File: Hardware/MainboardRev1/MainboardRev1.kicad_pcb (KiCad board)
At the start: 2 copper layers, 92 x 92 mm, 202 parts, among them J1 MAIN_BATT: 1586038-2, J10 Switch_3, J11 Switch_2, J12 Switch_4, J2 BACKUP_BATT: 1586038-2, J3 Servo_Control, J4 EMATCH_1: 1586038-2, J5 EMATCH_2: 1586038-2, J6 Stratologger_PWR: 1586038-2, J7 Stratologger_DATA, J8 0733910320 [915MHz SMA], J9 Switch_1, Q1 SSM3J328R, Q10 SSM3J328R, Q11 NTR4003, Q12 NTR4003, Q13 NTR4003, Q14 SSM3J328R, Q15 NTR4003, Q16 SSM3J328R, Q17 SSM3J328R, Q18 NTR4003, Q19 NTR4003, Q2 SSM3J328R, Q20 SIS612EDNT-T1-GE3, Q21 SIS612EDNT-T1-GE3, Q22 NTR4003, Q23 NTR4003, Q24 NTR4003, Q25 SSM3J328R, Q26 NTR4003, Q3 SSM3J328R, Q4 SSM3J328R, Q5 NTR4003, Q6 NTR4003, Q7 NTR4003, Q8 SSM3J328R, Q9 NTR4003, SW1 EG2201A [DPDT], U1 LT6703-3, U10 LTC4358, U11 Teensy3.6, U12 ABPMANN030PG2A3, U13 LSM9DS1, U14 LIS331HH, U15 BME280, U16 CCS811, U17 ublox_max-m8q, U18 RFM69HCW, U2 LTC3605, U3 LTC4358, U4 LTC4358, U5 LDL1117S50R, U6 LDL1117S33R, U7 LTC2992, U8 LDL1117S33R, U9 LTC2992

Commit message: Components placed. Needs to be routed.
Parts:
- removed C1: 47uF, Capacitors_SMD:C_1210_HandSoldering
- added C36: 10nF, Capacitors_SMD:C_0603_HandSoldering, B.Cu at (72.4, 80.0)
- added J13: EXTRA_5V, Dans_Parts:CONN_2POS_VERT_TE_CONN_LOCK_5-103669-1, F.Cu at (114.7, 110.7)
- added J14: EXTRA_3V3, Dans_Parts:CONN_2POS_VERT_TE_CONN_LOCK_5-103669-1, F.Cu at (114.7, 119.5)
- added MH1: Mounting Hole, Dans_Parts:Mounting_Hole_3.50mm, F.Cu at (54.0, 62.0)
- added MH2: Mounting Hole, Dans_Parts:Mounting_Hole_3.50mm, F.Cu at (138.0, 62.0)
- added MH3: Mounting Hole, Dans_Parts:Mounting_Hole_3.50mm, F.Cu at (54.0, 130.0)
- added MH4: Mounting Hole, Dans_Parts:Mounting_Hole_3.50mm, F.Cu at (138.0, 130.0)
- C10, C11, C12, C13, C2, C3, C33, C34, C35, C4, C5, C6, C7, C8, C9, D1, D11, D2, D3, D4, D5, L1, Q1, Q10, Q11, Q12, Q13, Q14, Q15, Q2, Q3, Q4, Q5, Q6, Q7, Q8, R1, R10, R11, R12, R13, R14, R15, R16, R17, R18, R19, R2, R21, R22, R23, R25, R28, R3, R34, R4, R44, R45, R5, R6, R7, R78, R8, R84, R85, R86, R87, R88, R89, R9, R90, R91, U1, U2, U3, U4: moved to B.Cu
- C14, C19: value 1uF -> 47uF; footprint Capacitors_SMD:C_0603_HandSoldering -> Capacitors_SMD:C_1210_HandSoldering; moved to B.Cu
- C15, C20: value 4.7uF -> 0.1uF
- C16, C17, C18, C21: value 4.7uF -> 47uF; footprint Capacitors_SMD:C_0603_HandSoldering -> Capacitors_SMD:C_1210_HandSoldering; moved to B.Cu
- C23: value 10000pF -> 47uF; footprint Capacitors_SMD:C_0603_HandSoldering -> Capacitors_SMD:C_1210_HandSoldering; moved to B.Cu
- C24: value 0.1uF -> 10000pF
- C25: value 100nF -> 0.1uF
- C26: value 0.1uF -> 100nF
- C32: value 10nF -> 0.1uF
- J1: value MAIN_BATT: 1586038-2 -> BACKUP_BATT: 1586038-2
- J10, J11, J12, J9: footprint Dans_Parts:Molex_Microfit3_Header_02x01_Straight -> Dans_Parts:CONN_2POS_VERT_TE_CONN_LOCK_5-103669-1
- J2: value BACKUP_BATT: 1586038-2 -> MAIN_BATT: 1586038-2
- R56: value 10k -> 45.2k; moved to B.Cu
- R57: value 45.2k -> 11.3k; moved to B.Cu
- R58: value 11.3k -> R
- R59: value 10k -> R
- R60: value 45.2k -> R
- R61, R66: value 11.3k -> 45.2k; moved to B.Cu
- R62: value R -> 11.3k; moved to B.Cu
- R63, R64: value R -> 10k
- R65: value 45.2k -> 10k
- R67: value 10k -> 11.3k; moved to B.Cu
- U10: footprint Housings_SSOP:TSSOP-14-1EP_4.4x5mm_Pitch0.65mm -> Housings_SSOP:HTSSOP-16-1EP_4.4x5mm_Pitch0.65mm; moved to B.Cu
- U5, U6, U8: footprint TO_SOT_Packages_SMD:SOT-223 -> Dans_Parts:SOT-223_Tab_Pin_2; moved to B.Cu
- moved R76 270.0 mm to (52.8, 97.7), turned to 180 degrees
- moved R75 262.0 mm to (56.4, 100.8), turned to 270 degrees
- moved J7 259.1 mm to (60.4, 129.9), turned to 270 degrees
- moved C35 257.8 mm to (72.4, 87.7)
- moved R78 254.1 mm to (58.0, 126.6), turned to 90 degrees
- moved R77 253.8 mm to (56.4, 95.2), turned to 90 degrees
- moved Q25 251.5 mm to (53.3, 100.8), turned to 180 degrees
- moved Q26 251.2 mm to (53.3, 94.9), turned to 180 degrees
- moved R59 250.4 mm to (53.1, 72.4), turned to 180 degrees
- moved R89 249.9 mm to (72.4, 81.5)
- moved R84 249.5 mm to (79.8, 92.5), turned to 180 degrees
- moved R60 246.5 mm to (53.1, 78.0), turned to 180 degrees
- moved R86 245.6 mm to (79.8, 89.4), turned to 180 degrees
- moved C34 244.0 mm to (79.8, 83.6)
- moved R85 242.9 mm to (79.8, 85.1), turned to 180 degrees
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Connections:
- C14 pad 1: Net-(C14-Pad1) -> BATTERY_PWR_MSMT
- C15 pad 1: LDO_FEED -> Net-(C15-Pad1)
- C17 pad 1: +5V_MSMT -> LDO_FEED
- C18 pad 1: +3.3V_MSMT -> +5V_MSMT
- C19 pad 1: Net-(C19-Pad1) -> +3.3V_MSMT
- C2 pad 1: MAIN_BATT -> BACKUP_BATT
- C20 pad 1: STARTUP_BATT -> Net-(C20-Pad1)
- C21 pad 1: +3.3V_STARTUP -> STARTUP_BATT
- C22 pad 1: Net-(C22-Pad1) -> +3.3V_STARTUP
- C23 pad 1: LSM_CAP -> Net-(C23-Pad1)
- C24 pad 1: Net-(C24-Pad1) -> LSM_CAP
- C25 pad 1: LSM_C1 -> Net-(C25-Pad1)
- C26 pad 1: Net-(C26-Pad1) -> LSM_C1
- C3 pad 1: BACKUP_BATT -> MAIN_BATT
- D1 pad 1: MAIN_BATT -> BACKUP_BATT
- D10 pad 2: +5V -> Net-(D10-Pad2)
- D11 pad 1: Net-(C22-Pad1) -> Net-(C23-Pad1)
- D2 pad 1: BACKUP_BATT -> MAIN_BATT
- D6 pad 2: +5V -> Net-(D6-Pad2)
- J10 pad 1: Net-(C33-Pad1) -> Net-(C34-Pad1)
- J11 pad 1: Net-(C34-Pad1) -> Net-(C35-Pad1)
- J12 pad 1: Net-(C35-Pad1) -> Net-(C36-Pad1)
- J3 pad 2: Net-(C22-Pad1) -> Net-(C23-Pad1)
- J9 pad 1: Net-(C32-Pad1) -> Net-(C33-Pad1)
- Q1 pad 2: MAIN_BATT -> BACKUP_BATT
- Q12 pad 3: Net-(Q12-Pad3) -> Net-(D6-Pad1)
- Q13 pad 3: Net-(Q13-Pad3) -> Net-(D10-Pad1)
- Q2 pad 2: BACKUP_BATT -> MAIN_BATT
- Q3 pad 2: MAIN_BATT -> BACKUP_BATT
- Q4 pad 2: BACKUP_BATT -> MAIN_BATT
- Q5 pad 1: MAIN_BATT_EN -> BACKUP_BATT_EN
- Q6 pad 1: BACKUP_BATT_EN -> MAIN_BATT_EN
- R12 pad 1: MAIN_BATT_EN -> +3.3V_STARTUP
- R12 pad 2: GND -> BACKUP_BATT_EN
- R13 pad 1: +3.3V_STARTUP -> MAIN_BATT_EN
- R13 pad 2: BACKUP_BATT_EN -> GND
- R24 pad 1: Net-(C14-Pad1) -> Net-(C15-Pad1)
- R31 pad 1: Net-(C19-Pad1) -> Net-(C20-Pad1)
- R35 pad 1: +5V -> +3.3V
- R35 pad 2: +5V_MSMT -> +3.3V_MSMT
- R36 pad 1: +3.3V -> +5V
- R36 pad 2: +3.3V_MSMT -> +5V_MSMT
- R39 pad 1: Net-(D6-Pad1) -> +5V
- R39 pad 2: Net-(Q12-Pad3) -> Net-(D6-Pad2)
- R43 pad 1: Net-(D10-Pad1) -> +5V
- R43 pad 2: Net-(Q13-Pad3) -> Net-(D10-Pad2)
- R56 pad 1: +3.3V -> MAIN_BATT
- R56 pad 2: SENSORS_SCL -> MAIN_BATT_ANLG
- R57 pad 1: MAIN_BATT -> MAIN_BATT_ANLG
- R57 pad 2: MAIN_BATT_ANLG -> MAIN_BATT_READ_EN
- R58 pad 1: MAIN_BATT_ANLG -> Net-(D14-Pad2)
- R58 pad 2: MAIN_BATT_READ_EN -> +5V
- R59 pad 1: +3.3V -> Net-(D15-Pad2)
- R59 pad 2: SENSORS_SDA -> +5V
- R6 pad 1: MAIN_BATT -> BACKUP_BATT
- R60 pad 1: EMATCH_1_CHECK -> Net-(D16-Pad2)
- R60 pad 2: EMATCH_1_ANLG -> +5V
- R61 pad 1: EMATCH_1_ANLG -> EMATCH_1_CHECK
- R61 pad 2: GND -> EMATCH_1_ANLG
- R62 pad 1: Net-(D14-Pad2) -> EMATCH_1_ANLG
- R62 pad 2: +5V -> GND
- R63 pad 1: Net-(D15-Pad2) -> GND
- R63 pad 2: +5V -> LED_GREEN
- R64 pad 1: Net-(D16-Pad2) -> GND
- R64 pad 2: +5V -> LED_BLUE
- R65 pad 1: EMATCH_2_CHECK -> +3.3V
- R65 pad 2: EMATCH_2_ANLG -> LED_RED
- R66 pad 1: EMATCH_2_ANLG -> EMATCH_2_CHECK
- R66 pad 2: GND -> EMATCH_2_ANLG
- R67 pad 1: GND -> EMATCH_2_ANLG
- R67 pad 2: LED_GREEN -> GND
- R68 pad 1: GND -> +3.3V
- R68 pad 2: LED_BLUE -> SENSORS_SCL
- R69 pad 2: LED_RED -> SENSORS_SDA
- R70 pad 1: Net-(C24-Pad1) -> Net-(C25-Pad1)
- R71 pad 1: Net-(C26-Pad1) -> Net-(C27-Pad1)
- R72 pad 1: Net-(C27-Pad1) -> Net-(C28-Pad1)
- R73 pad 1: Net-(C28-Pad1) -> Net-(C29-Pad1)
- R74 pad 1: Net-(C29-Pad1) -> Net-(C30-Pad1)
- R79 pad 1: Net-(C30-Pad1) -> Net-(C31-Pad1)
- R8 pad 1: BACKUP_BATT -> MAIN_BATT
- R81 pad 1: Net-(C31-Pad1) -> Net-(C32-Pad1)
- R84 pad 2: Net-(C32-Pad1) -> Net-(C33-Pad1)
- R85 pad 2: Net-(C33-Pad1) -> Net-(C34-Pad1)
- R86 pad 2: Net-(C32-Pad1) -> Net-(C33-Pad1)
- R87 pad 2: Net-(C33-Pad1) -> Net-(C34-Pad1)
- R88 pad 2: Net-(C34-Pad1) -> Net-(C35-Pad1)
- R89 pad 2: Net-(C35-Pad1) -> Net-(C36-Pad1)
- R90 pad 2: Net-(C34-Pad1) -> Net-(C35-Pad1)
- R91 pad 2: Net-(C35-Pad1) -> Net-(C36-Pad1)
- U10 pad 10: Net-(U10-Pad10) -> Net-(C23-Pad1)
- U10 pad 11: Net-(Q14-Pad3) -> Net-(U10-Pad11)
- U10 pad 15: Net-(C22-Pad1) -> Net-(Q14-Pad3)
- U10 pad 7: GND -> Net-(U10-Pad7)
- U10 pad 8: Net-(C22-Pad1) -> GND
- U10 pad 9: Net-(C22-Pad1) -> Net-(C23-Pad1)
- U12 pad 2: Net-(C26-Pad1) -> Net-(C27-Pad1)
- U13 pad 1: Net-(C24-Pad1) -> Net-(C25-Pad1)
- U13 pad 22: Net-(C24-Pad1) -> Net-(C25-Pad1)
- U13 pad 23: Net-(C24-Pad1) -> Net-(C25-Pad1)
- U13 pad 3: Net-(C24-Pad1) -> Net-(C25-Pad1)
- U14 pad 1: Net-(C27-Pad1) -> Net-(C28-Pad1)
- U14 pad 14: Net-(C27-Pad1) -> Net-(C28-Pad1)
- U14 pad 15: Net-(C27-Pad1) -> Net-(C28-Pad1)
- U15 pad 2: Net-(C28-Pad1) -> Net-(C29-Pad1)
- U15 pad 6: Net-(C28-Pad1) -> Net-(C29-Pad1)
- U15 pad 8: Net-(C28-Pad1) -> Net-(C29-Pad1)
- U16 pad 6: Net-(C29-Pad1) -> Net-(C30-Pad1)
- U17 pad 6: Net-(C30-Pad1) -> Net-(C31-Pad1)
- U17 pad 7: Net-(C30-Pad1) -> Net-(C31-Pad1)
- U17 pad 8: Net-(C30-Pad1) -> Net-(C31-Pad1)
- U17 pad 9: Net-(C30-Pad1) -> Net-(C31-Pad1)
- U18 pad 13: Net-(C31-Pad1) -> Net-(C32-Pad1)
- U3 pad 10: Net-(U3-Pad10) -> BATTERY_PWR_MSMT
- U3 pad 11: Net-(Q3-Pad3) -> Net-(U3-Pad11)
- U3 pad 15: BATTERY_PWR_MSMT -> Net-(Q3-Pad3)
- U3 pad 16: (no net) -> Net-(Q3-Pad3)
- U3 pad 17: (no net) -> BATTERY_PWR_MSMT
- U3 pad 7: GND -> Net-(U3-Pad7)
- U3 pad 8: BATTERY_PWR_MSMT -> GND
- U4 pad 10: Net-(U4-Pad10) -> BATTERY_PWR_MSMT
- U4 pad 11: Net-(Q4-Pad3) -> Net-(U4-Pad11)
- U4 pad 15: BATTERY_PWR_MSMT -> Net-(Q4-Pad3)
- U4 pad 16: (no net) -> Net-(Q4-Pad3)
- U4 pad 17: (no net) -> BATTERY_PWR_MSMT
- U4 pad 7: GND -> Net-(U4-Pad7)
- U4 pad 8: BATTERY_PWR_MSMT -> GND
- U7 pad 7: Net-(C14-Pad1) -> Net-(C15-Pad1)
- U7 pad 8: Net-(C14-Pad1) -> Net-(C15-Pad1)
- U9 pad 1: +5V -> +3.3V
- U9 pad 15: +3.3V_MSMT -> +5V_MSMT
- U9 pad 16: +3.3V -> +5V
- U9 pad 2: +5V_MSMT -> +3.3V_MSMT
- U9 pad 7: Net-(C19-Pad1) -> Net-(C20-Pad1)
- U9 pad 8: Net-(C19-Pad1) -> Net-(C20-Pad1)
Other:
- outline, holes or cut-outs redrawn
- copper layers 2 -> 4
- net class 5A_External added: clearance 0.2, trace_width 1.4, via_dia 0.6, via_drill 0.4
- board text added: "3.3V"
- board text added: "5V"
- board text added: "6.5V"
- board text added: "915 MHz ANT"
- board text added: "Backup Batt"
- board text added: "Batt"
- board text added: "Ematch 1 ARMED"
- board text added: "Ematch 2 ARMED"
- board text added: "Extra 3V3"
- board text added: "Extra 5V"
- board text added: "GPS Lock"
- board text added: "Main Batt"
- board text added: "OFF"
- board text added: "ON"
- board text added: "SW1"
- board text added: "SW2"
- board text added: "SW3"
- board text added: "SW4"
- board text added: "Servo Motor"
- board text added: "Strato Data"
- board text added: "Strato Power"

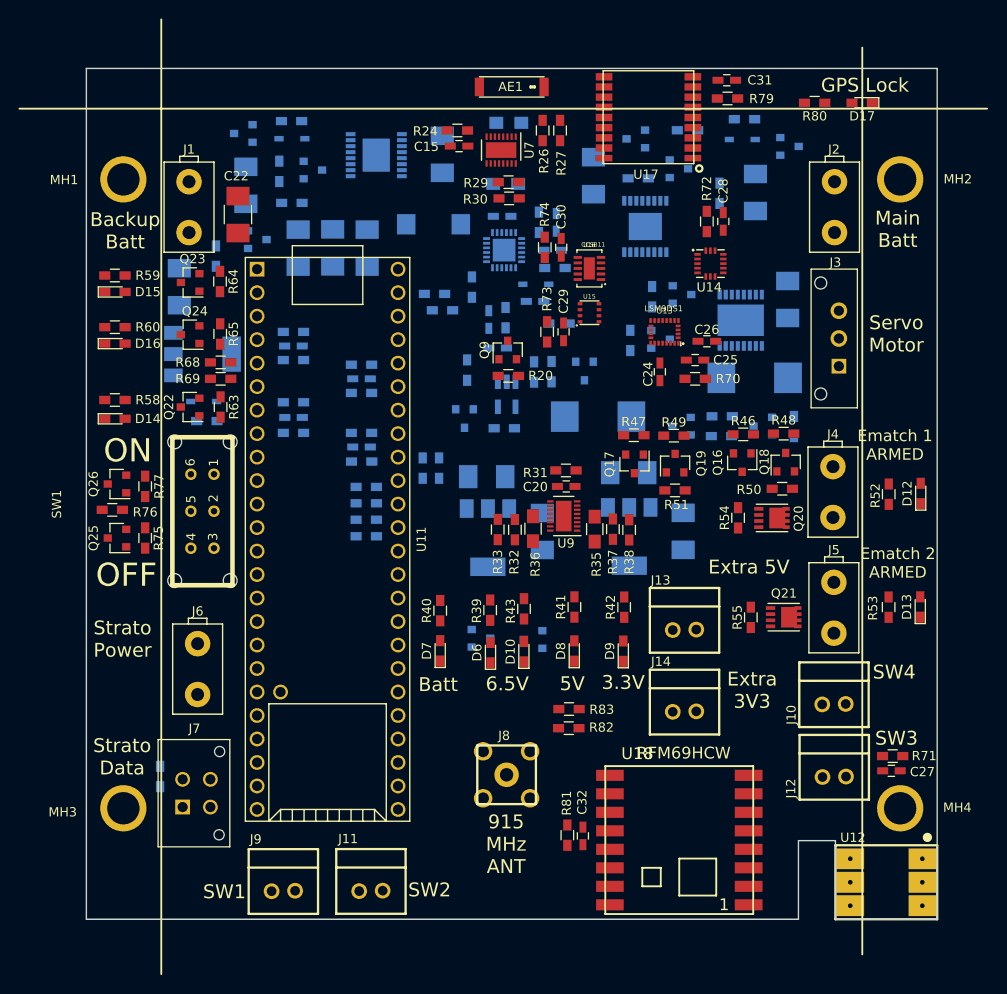
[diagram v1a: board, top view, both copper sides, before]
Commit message: Added to silkscreen. Updated schematic pdf
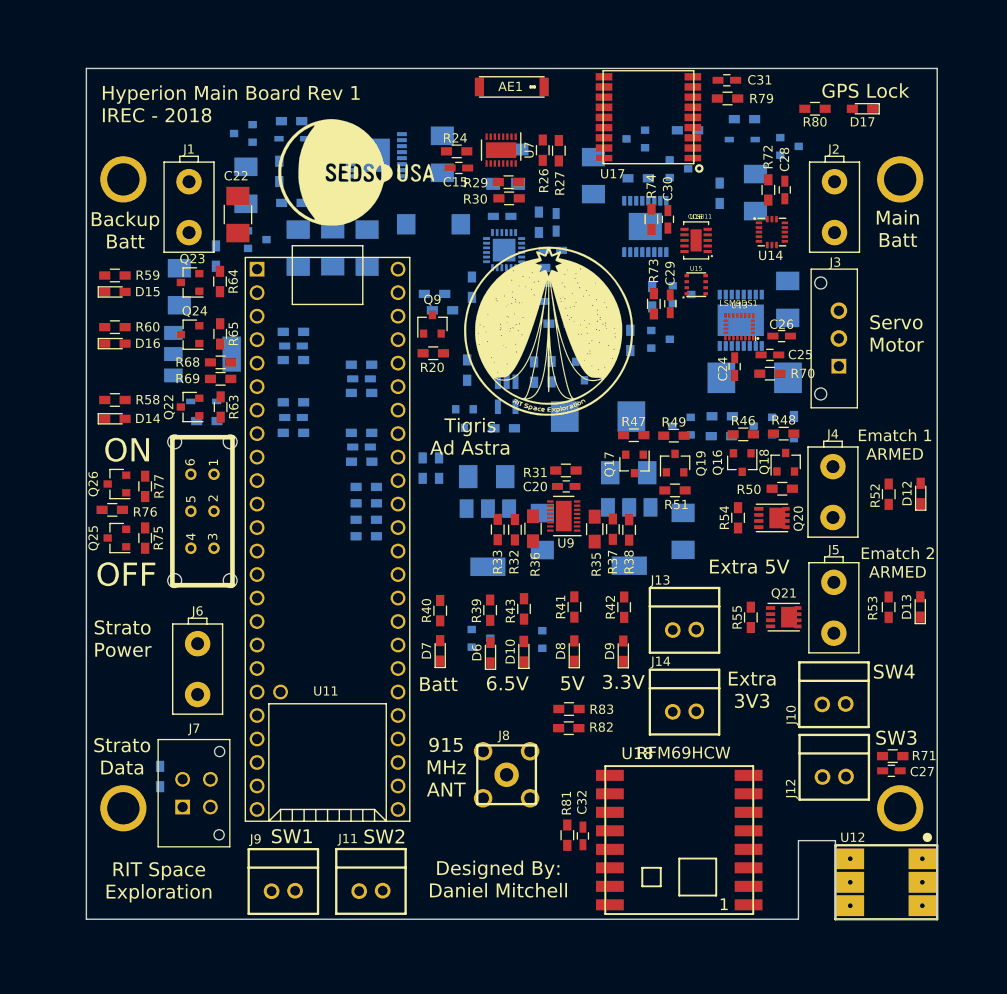
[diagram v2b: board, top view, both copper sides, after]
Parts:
- added G***: LOGO, Media:SPEX_KiCAD_footprint, F.Cu at (100.0, 78.4)
- added G***: LOGO, Media:SEDS_KiCAD_footprint, F.Cu at (79.1, 61.2)
- moved C29 11.9 mm to (113.1, 75.5)
- moved R74 11.9 mm to (111.1, 66.3)
- moved U15 11.9 mm to (114.9, 72.4)
- moved C30 11.9 mm to (112.9, 66.3)
- moved R73 11.9 mm to (111.4, 75.5)
- moved U16 11.9 mm to (115.9, 68.6)
- moved Q9 8.60 mm to (87.4, 77.7)
- moved R20 8.48 mm to (87.5, 80.8)
- moved C24 8.11 mm to (120.1, 82.2)
- moved C25 8.11 mm to (123.9, 81.0)
- moved C26 8.11 mm to (125.2, 78.9)
- moved R70 8.11 mm to (123.9, 83.0)
- moved U13 8.11 mm to (120.6, 77.9)
- moved C28 7.47 mm to (125.5, 63.1)
- moved R72 7.47 mm to (123.7, 63.1)
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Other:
- board text added: "Designed By: Daniel Mitchell"
- board text added: "Hyperion Main Board Rev 1 IREC - 2018"
- board text added: "RIT Space Exploration"
- board text added: "Tigris Ad Astra"
